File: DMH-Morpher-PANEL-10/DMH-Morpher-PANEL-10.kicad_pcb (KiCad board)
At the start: 2 copper layers, 100 x 200 mm, 29 parts, among them J0 Panel_GND_Solder_Wire_Pad

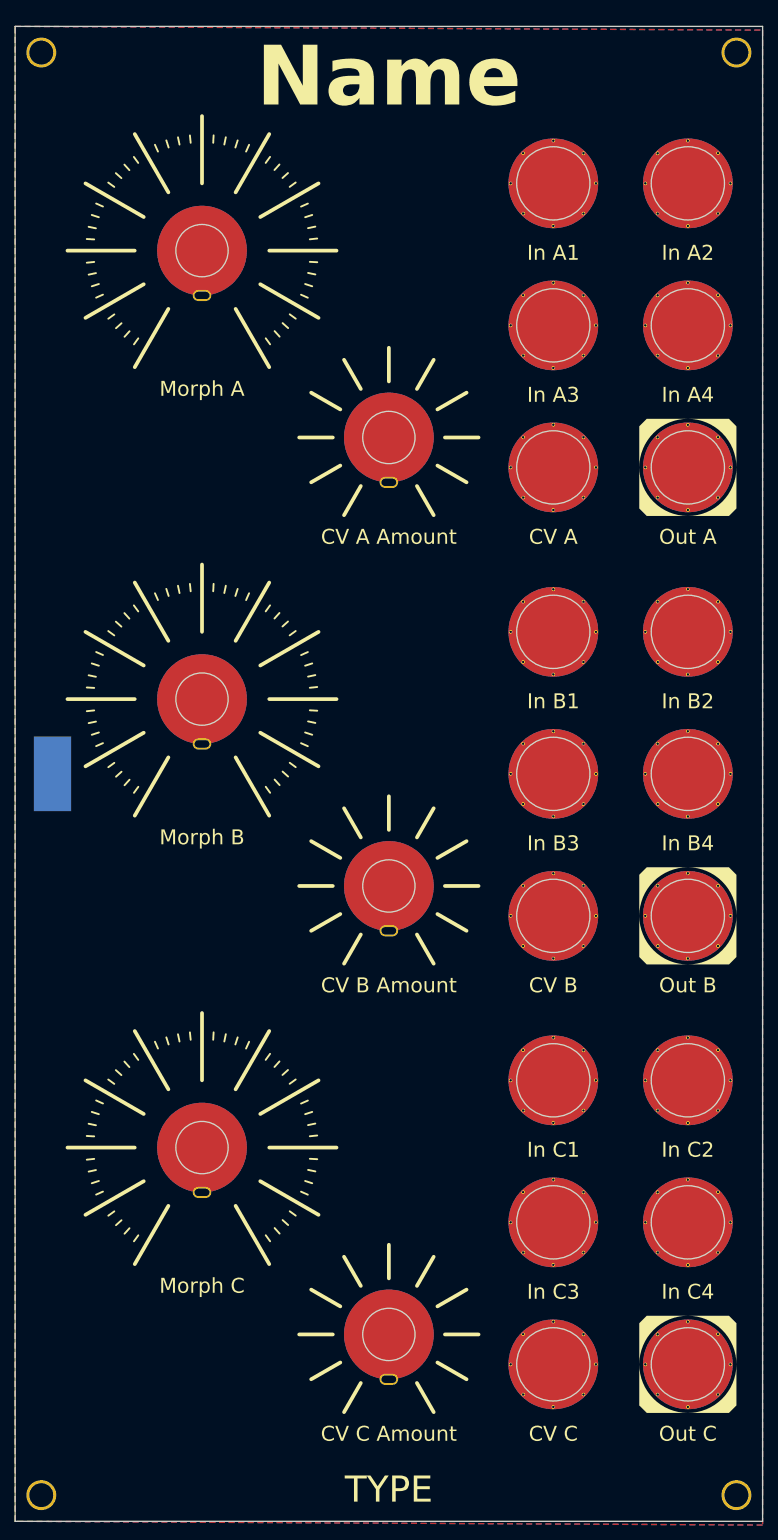
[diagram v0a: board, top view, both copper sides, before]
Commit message: Made 10cm panel
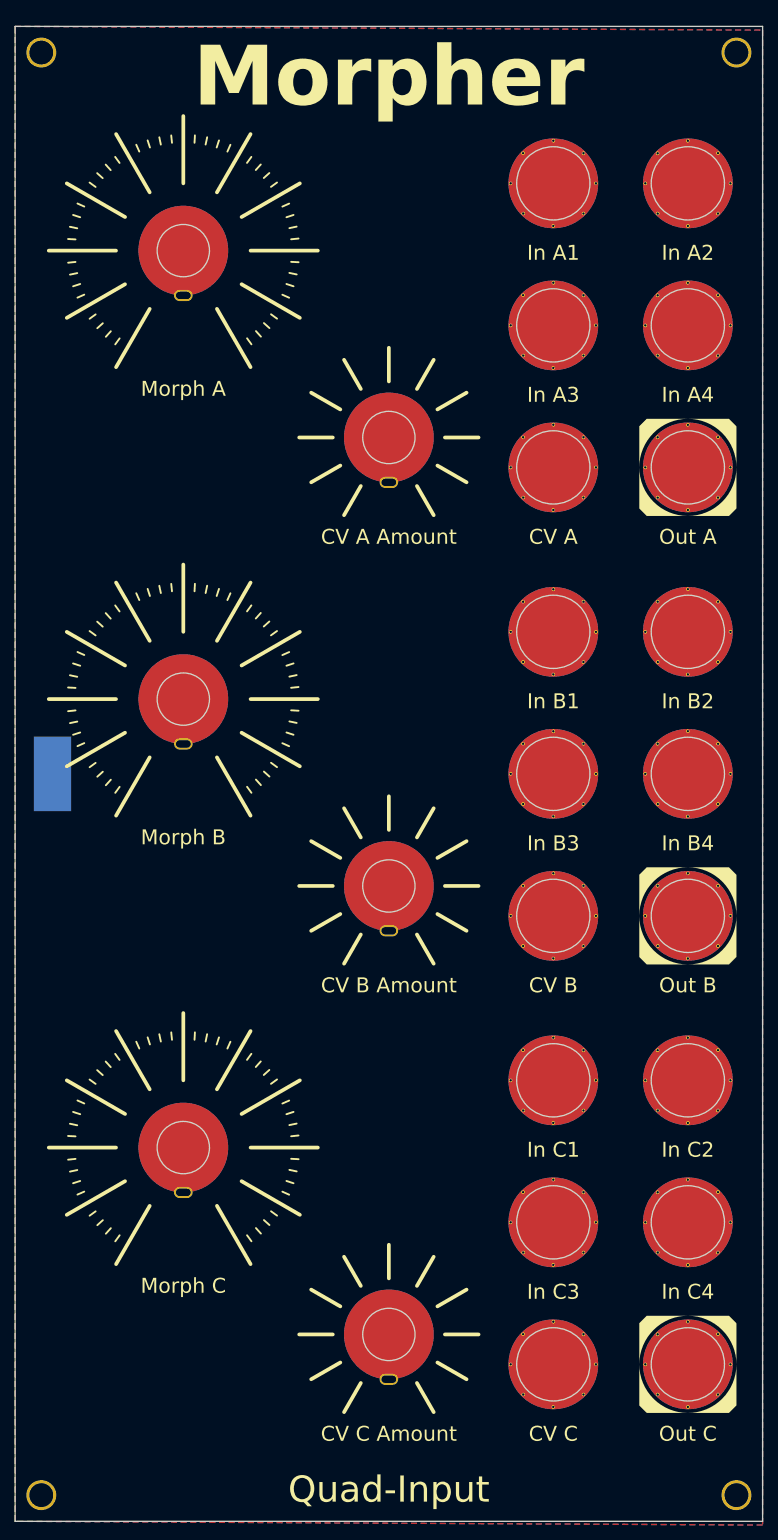
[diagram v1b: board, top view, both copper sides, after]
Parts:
- moved H10 2.50 mm to (72.5, 120.0)
- moved H23 2.50 mm to (72.5, 180.0)
- moved H7 2.50 mm to (72.5, 60.0)
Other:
- board text added: "Morpher"
- board text added: "Quad-Input"
- board text removed: "Name"
- board text removed: "TYPE"

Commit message: Front panel art ongoing
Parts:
- moved H7 0.50 mm to (72.5, 60.5)

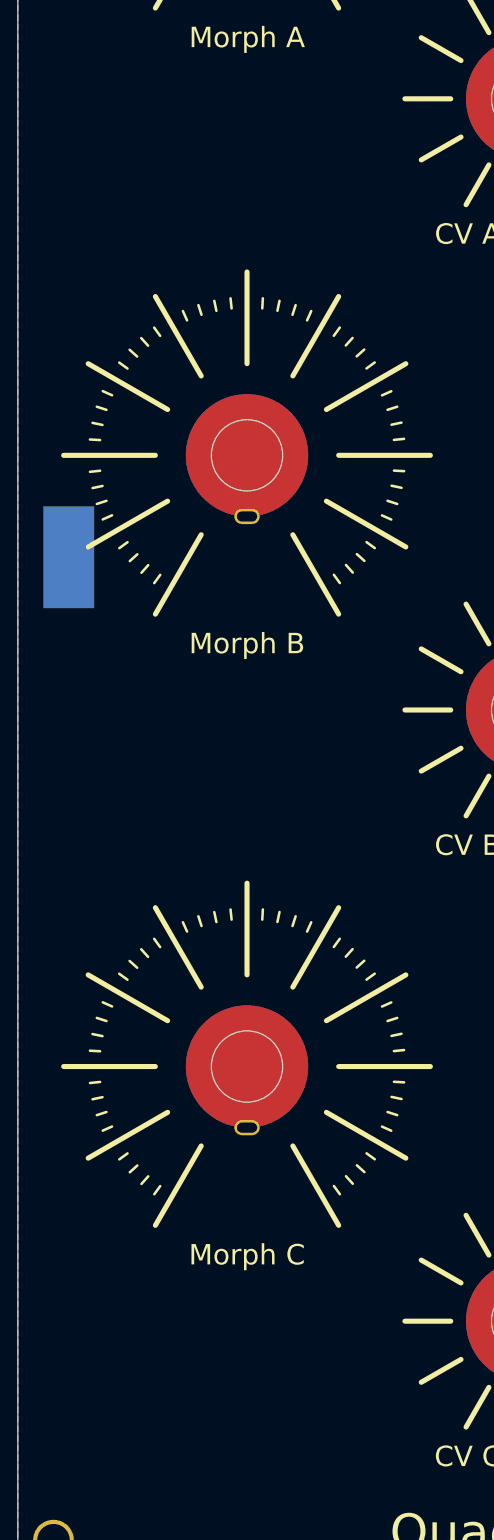
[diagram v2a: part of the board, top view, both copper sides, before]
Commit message: Finished 10cm front panel
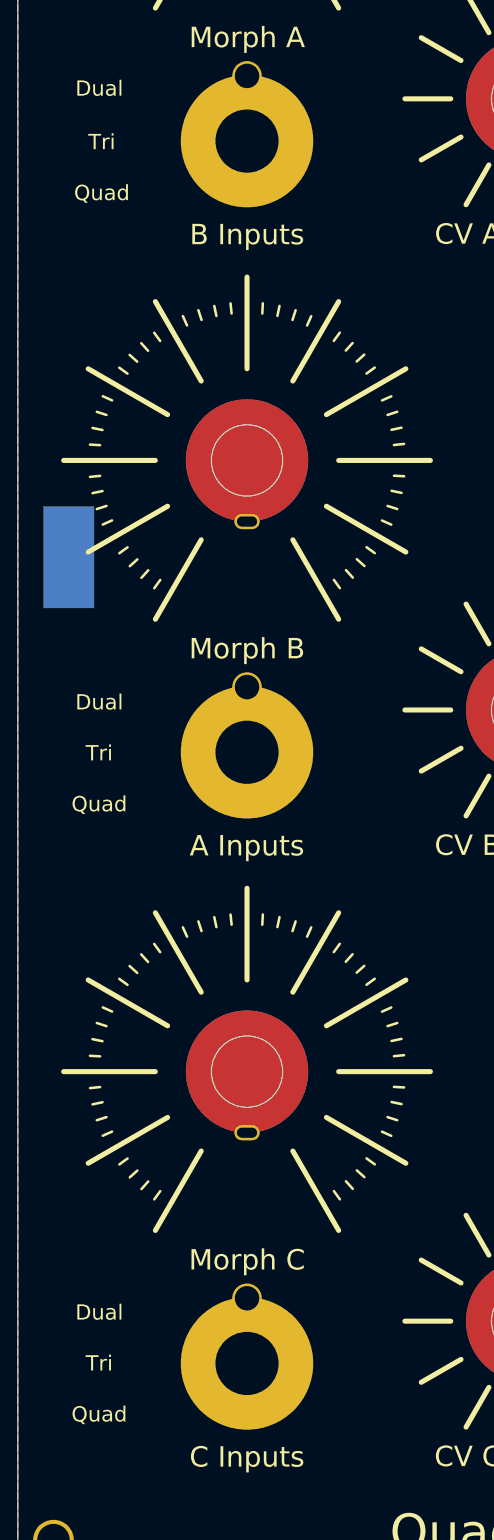
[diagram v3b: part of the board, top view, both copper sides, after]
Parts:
- added H29: A Inputs, SynthStuff:Toggle_Switch_Cutout, F.Cu at (72.5, 149.2)
- added H30: B Inputs, SynthStuff:Toggle_Switch_Cutout, F.Cu at (72.5, 89.2)
- added H31: C Inputs, SynthStuff:Toggle_Switch_Cutout, F.Cu at (72.5, 209.2)
- moved H10 0.50 mm to (72.5, 120.5)
- moved H23 0.50 mm to (72.5, 180.5)
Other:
- board text added: "Dual"
- board text added: "Quad"
- board text added: "Tri"

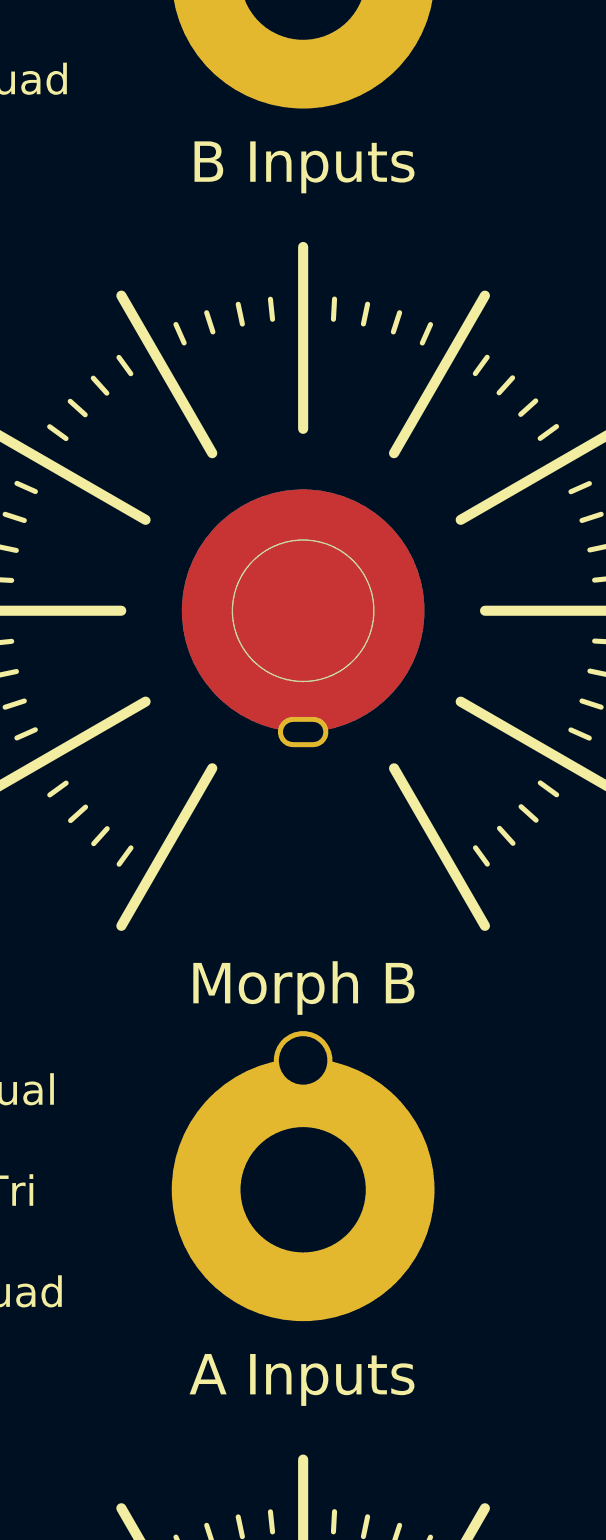
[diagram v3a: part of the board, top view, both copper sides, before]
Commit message: Started 10cm module PCB
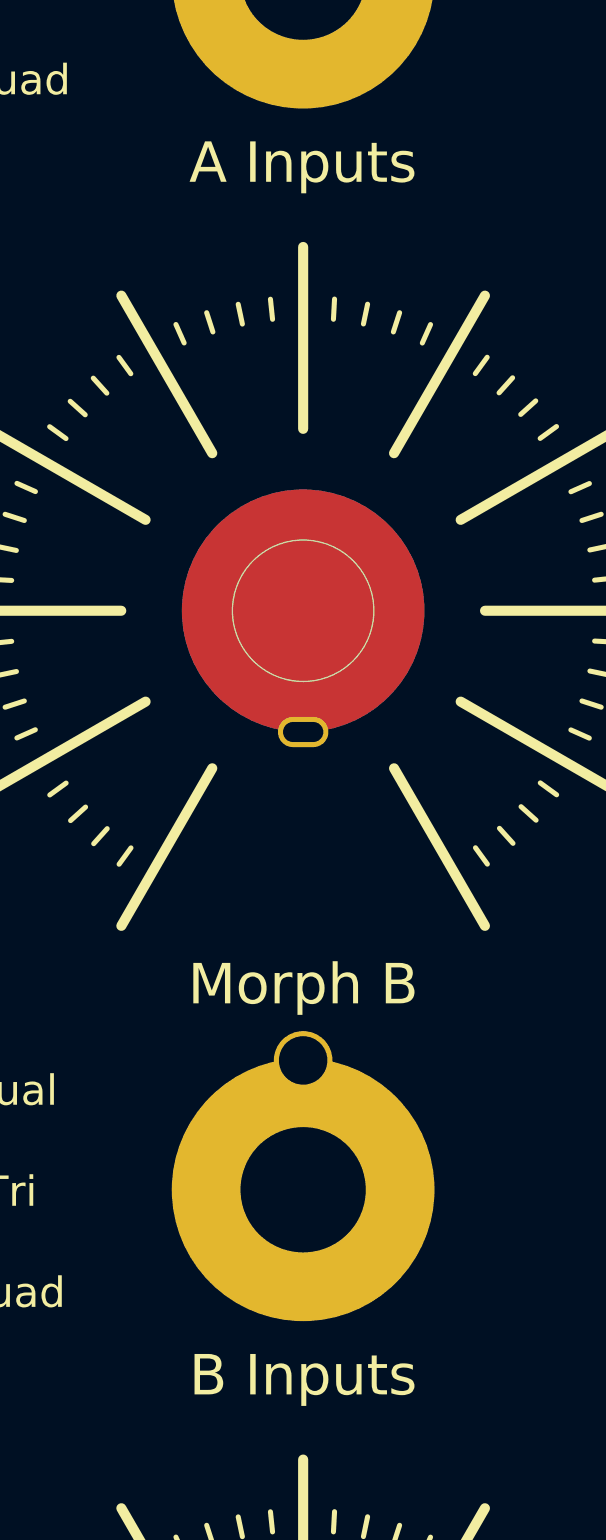
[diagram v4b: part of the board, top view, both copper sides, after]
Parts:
- moved H29 60.0 mm to (72.5, 89.2)
- moved H30 60.0 mm to (72.5, 149.2)

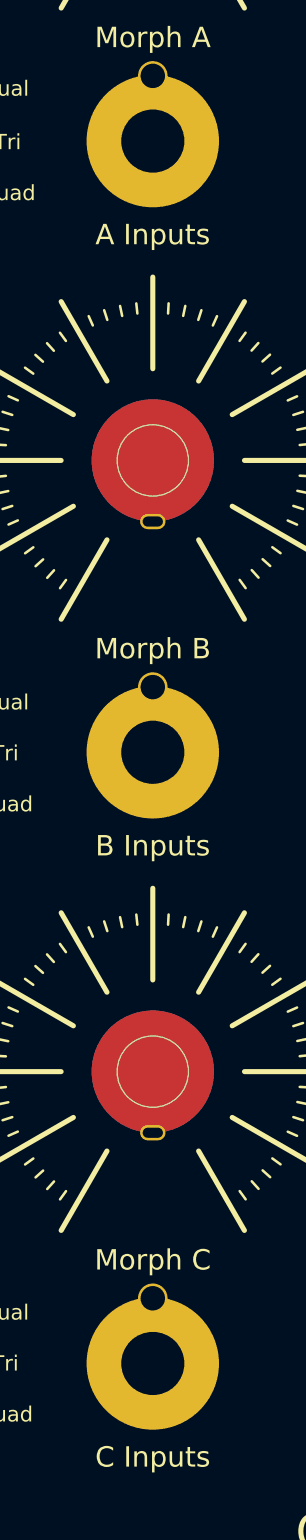
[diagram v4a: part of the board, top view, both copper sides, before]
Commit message: Centralized library location
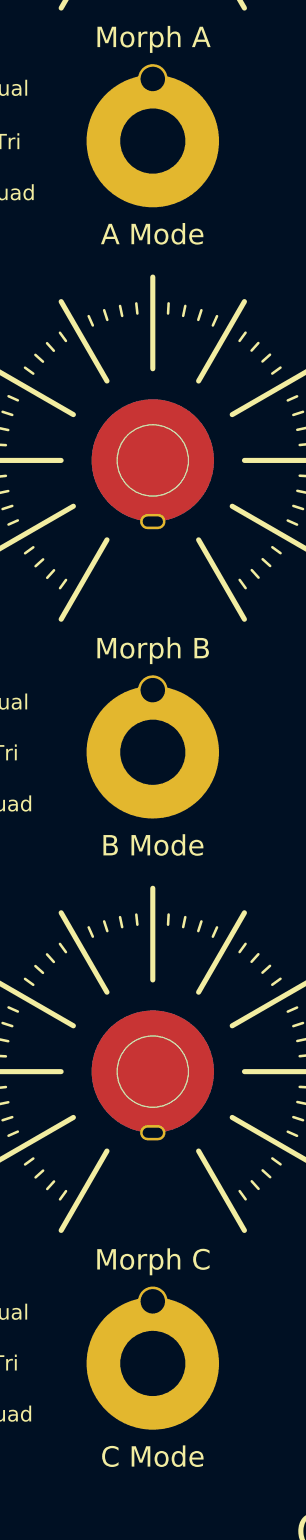
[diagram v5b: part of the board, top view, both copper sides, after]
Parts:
- H29: value A Inputs -> A Mode; footprint SynthStuff:Toggle_Switch_Cutout -> SynthStuff:Toggle_Switch_TE_Cutout
- H30: value B Inputs -> B Mode; footprint SynthStuff:Toggle_Switch_Cutout -> SynthStuff:Toggle_Switch_TE_Cutout
- H31: value C Inputs -> C Mode; footprint SynthStuff:Toggle_Switch_Cutout -> SynthStuff:Toggle_Switch_TE_Cutout
